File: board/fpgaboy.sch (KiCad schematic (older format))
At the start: 83 parts, among them J1 Conn_01x12, J2 Conn_01x06, J3 Micro_SD_Card_Det, J4 Conn_01x06, P1 ILI9341, P2 CONN_01X02, P3 USB_OTG, Q1 BSS816NW, SW1 SWITCH_SPST, U1 iCE40-HX8k-BG121, U2 DSC60XX, U3 GS74116AGP/, U4 BQ21040, U5 NCP1532, U6 SAML22G18A

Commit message: Connect LCD interface
Former-commit-id: be222472ea62f5be4bca7c37730c00a19e503cfb [formerly a5ab949512d659eb4659003014dfb4631add8347]
Former-commit-id: 3fc0e25a0825eb883327bfa558efda45d3fda1b2
Former-commit-id: fb121b735d250eeeb6fec0ec3e54c77ea9ad060c
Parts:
- added TP15: TestPoint, fpgaboy_parts:Testpoint_d0.7mm, symbol Connector:TestPoint
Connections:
- net labels added: LCD_D~C~
- net labels removed: LCD_D/C
- wire segments 543 -> 544
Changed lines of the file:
@@
 LCD_SCL
 Text Label 1750 8800 2    59   ~ 0
-LCD_D/C
+LCD_D~C~
 Text Label 1750 8900 2    59   ~ 0
 LCD_CS
@@
 Text Label 3300 1500 2    60   ~ 0
 SRAM_A17
+Text Label 1350 4650 2    59   ~ 0
+LCD_RESET
+Text Label 1350 4550 2    59   ~ 0
+LCD_SCL
 Text Label 1350 4350 2    59   ~ 0
-LCD_RESET
+LCD_D~C~
+Text Label 1350 4250 2    59   ~ 0
+LCD_CS
 Text Label 1350 4450 2    59   ~ 0
-LCD_SCL
-Text Label 1350 4550 2    59   ~ 0
-LCD_D/C
-Text Label 1350 4650 2    59   ~ 0
-LCD_CS
+LCD_SDA
 Text Label 1350 4750 2    59   ~ 0
-LCD_SDA
-Text Label 1350 4850 2    59   ~ 0
 LCD_SDO
 Wire Wire Line
@@
 Wire Wire Line
 	1550 4250 1350 4250
-Text Label 1350 4250 2    50   ~ 0
+Text Label 1350 4850 2    50   ~ 0
 LCD_PWM
 Wire Wire Line
@@
 Wire Wire Line
 	3700 8950 3650 8950
-Text Label 3650 8650 2    59   ~ 0
-LCD_D/C
 Text Label 3650 8800 2    59   ~ 0
 LCD_CS
@@
 Text Notes 2900 7250 0    50   ~ 0
 Note there is extensive scrambling here\nto decongest FPGA->SRAM routing
+Text Label 3650 8650 2    59   ~ 0
+LCD_D~C~
+$Comp
+L Connector:TestPoint TP15
+U 1 1 5C00C5C4
+P 3700 8350
+F 0 "TP15" V 3654 8538 50  0000 L CNN
+F 1 "TestPoint" V 3745 8538 50  0000 L CNN
+F 2 "fpgaboy_parts:Testpoint_d0.7mm" H 3900 8350 50  0001 C CNN
+F 3 "~" H 3900 8350 50  0001 C CNN
+	1    3700 8350
+	0    1    1    0
+$EndComp
+Wire Wire Line
+	3700 8350 3650 8350
+Text Label 3650 8350 2    50   ~ 0
+LCD_RESET
 $EndSCHEMATC

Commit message: More routing
Former-commit-id: bc991a0f209c43e02855cfda4d759da6902f93c3 [formerly 65e1dfea039ff2136dd6c1c80006c66a69c9e176]
Former-commit-id: 8db9430dbe284821421561ad36d1d29c18d5a661
Former-commit-id: a4f765c582eb59d9cabff1b7e73d9f24a90fca27
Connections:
- net labels removed: FPGA_CFG_SO
- wire segments 544 -> 542
- no-connect marks 52 -> 54
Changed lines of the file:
@@
 Text Label 14650 8250 0    50   ~ 0
 USB_DP
-Text Label 5300 4850 2    50   ~ 0
-FPGA_CFG_SO
 Text Label 14650 7350 0    50   ~ 0
 FPGA_CFG_SI
@@
 Text Label 14650 7250 0    50   ~ 0
 FPGA_CFG_~RST
-Text Label 14650 7650 0    50   ~ 0
-FPGA_CFG_SO
 Wire Wire Line
 	14500 7350 14650 7350
@@
 Wire Wire Line
 	14500 7550 14650 7550
-Wire Wire Line
-	14500 7650 14650 7650
 NoConn ~ 14500 5750
 NoConn ~ 14500 5850
@@
 Wire Wire Line
 	5300 5150 5700 5150
-Wire Wire Line
-	5300 4850 6100 4850
 Connection ~ 5400 4650
 Wire Wire Line
@@
 Text Label 3650 8350 2    50   ~ 0
 LCD_RESET
+NoConn ~ 6100 4850
+NoConn ~ 14500 7650
 $EndSCHEMATC

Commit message: Update PDF following pinswapping for PCB
Former-commit-id: 44465b9019a83987ad1aa7dea38d15964084dbf7 [formerly 5f61d778534b163e39ed3c2f344e42ac27f538fd]
Former-commit-id: da721d4d19a2e198d24fefeb88b35d12907259f9
Former-commit-id: 9a12214701f09df0a8f4dc57eea492204a0ea488
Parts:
- J2, J4: footprint Connector_PinHeader_1.27mm:PinHeader_1x06_P1.27mm_Vertical -> Connector_PinHeader_2.54mm:PinHeader_1x06_P2.54mm_Vertical
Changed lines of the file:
@@
 F 0 "J4" H 6600 10200 50  0000 L CNN
 F 1 "Conn_01x06" V 6700 10350 50  0000 L CNN
-F 2 "Connector_PinHeader_1.27mm:PinHeader_1x06_P1.27mm_Vertical" H 6600 10600 50  0001 C CNN
+F 2 "Connector_PinHeader_2.54mm:PinHeader_1x06_P2.54mm_Vertical" H 6600 10600 50  0001 C CNN
 F 3 "~" H 6600 10600 50  0001 C CNN
 	1    6600 10600
@@
 F 0 "J2" H 6600 9250 50  0000 L CNN
 F 1 "Conn_01x06" V 6700 9400 50  0000 L CNN
-F 2 "Connector_PinHeader_1.27mm:PinHeader_1x06_P1.27mm_Vertical" H 6600 9650 50  0001 C CNN
+F 2 "Connector_PinHeader_2.54mm:PinHeader_1x06_P2.54mm_Vertical" H 6600 9650 50  0001 C CNN
 F 3 "~" H 6600 9650 50  0001 C CNN
 	1    6600 9650

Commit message: Correct orientation of LCD connector (oops), and add rudimentary audio to board.
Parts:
- added C30: 0.1u, Capacitor_SMD:C_0603_1608Metric, symbol fpgaboy-rescue:C
- added P4: CONN_01X02, Connector_PinHeader_2.54mm:PinHeader_1x02_P2.54mm_Vertical, symbol fpgaboy-rescue:CONN_01X02
- added R13, R15: 680, Resistor_SMD:R_0603_1608Metric, symbol fpgaboy-rescue:R
- added R14: 220, Resistor_SMD:R_0603_1608Metric, symbol fpgaboy-rescue:R
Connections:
- net labels added: AUDIO_PWM
- wire segments 542 -> 559
- no-connect marks 54 -> 53
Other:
- note added: "parallel resistors are just to\navoid more unique values\n"
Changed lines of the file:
@@
 Text Label 1750 8600 2    59   ~ 0
 LCD_RESET
-Text Label 1750 8700 2    59   ~ 0
+Text Label 1750 9100 2    59   ~ 0
 LCD_SCL
-Text Label 1750 8800 2    59   ~ 0
+Text Label 1750 9000 2    59   ~ 0
 LCD_D~C~
 Text Label 1750 8900 2    59   ~ 0
 LCD_CS
-Text Label 1750 9000 2    59   ~ 0
+Text Label 1750 8800 2    59   ~ 0
 LCD_SDA
-Text Label 1750 9100 2    59   ~ 0
+Text Label 1750 8700 2    59   ~ 0
 LCD_SDO
 Text Notes 1600 8000 0    59   ~ 0
@@
 	1    0    0    -1
 $EndComp
-NoConn ~ 1550 4950
 NoConn ~ 1550 5050
 Wire Wire Line
@@
 NoConn ~ 6100 4850
 NoConn ~ 14500 7650
+Wire Wire Line
+	1550 4950 1350 4950
+Text Label 1350 4950 2    50   ~ 0
+AUDIO_PWM
+$Comp
+L fpgaboy-rescue:CONN_01X02 P4
+U 1 1 5C08551B
+P 11000 7950
+F 0 "P4" H 11000 8100 50  0000 C CNN
+F 1 "CONN_01X02" V 11100 7950 50  0000 C CNN
+F 2 "Connector_PinHeader_2.54mm:PinHeader_1x02_P2.54mm_Vertical" H 11000 7950 50  0001 C CNN
+F 3 "" H 11000 7950 50  0000 C CNN
+	1    11000 7950
+	1    0    0    -1
+$EndComp
+Wire Wire Line
+	10800 8000 10700 8000
+$Comp
+L fpgaboy-rescue:GND #PWR0102
+U 1 1 5C0DBD8A
+P 10700 8500
+F 0 "#PWR0102" H 10700 8250 50  0001 C CNN
+F 1 "GND" H 10705 8327 50  0000 C CNN
+F 2 "" H 10700 8500 50  0000 C CNN
+F 3 "" H 10700 8500 50  0000 C CNN
+	1    10700 8500
+	1    0    0    -1
+$EndComp
+$Comp
+L fpgaboy-rescue:R R15
+U 1 1 5C133D1D
+P 10400 7650
+F 0 "R15" V 10480 7650 50  0000 C CNN
+F 1 "680" V 10400 7650 50  0000 C CNN
+F 2 "Resistor_SMD:R_0603_1608Metric" V 10330 7650 50  0001 C CNN
+F 3 "" H 10400 7650 50  0000 C CNN
+	1    10400 7650
+	1    0    0    -1
+$EndComp
+$Comp
+L fpgaboy-rescue:R R13
+U 1 1 5C1342F3
+P 10150 7650
+F 0 "R13" V 10230 7650 50  0000 C CNN
+F 1 "680" V 10150 7650 50  0000 C CNN
+F 2 "Resistor_SMD:R_0603_1608Metric" V 10080 7650 50  0001 C CNN
+F 3 "" H 10150 7650 50  0000 C CNN
+	1    10150 7650
+	1    0    0    -1
+$EndComp
+$Comp
+L fpgaboy-rescue:R R14
+U 1 1 5C18A52F
+P 10150 8150
+F 0 "R14" V 10230 8150 50  0000 C CNN
+F 1 "220" V 10150 8150 50  0000 C CNN
+F 2 "Resistor_SMD:R_0603_1608Metric" V 10080 8150 50  0001 C CNN
+F 3 "" H 10150 8150 50  0000 C CNN
+	1    10150 8150
+	1    0    0    -1
+$EndComp
+$Comp
+L fpgaboy-rescue:C C30
+U 1 1 5C18A953
+P 10400 8150
+F 0 "C30" H 10425 8250 50  0000 L CNN
+F 1 "0.1u" H 10425 8050 50  0000 L CNN
+F 2 "Capacitor_SMD:C_0603_1608Metric" H 10438 8000 50  0001 C CNN
+F 3 "" H 10400 8150 50  0000 C CNN
+	1    10400 8150
+	1    0    0    -1
+$EndComp
+Wire Wire Line
+	10150 7800 10150 7900
+Wire Wire Line
+	10400 7800 10400 7900
+Wire Wire Line
+	10400 7900 10800 7900
+Connection ~ 10400 7900
+Wire Wire Line
+	10400 7900 10400 8000
+Wire Wire Line
+	10400 7900 10150 7900
+Connection ~ 10150 7900
+Wire Wire Line
+	10150 7900 10150 8000
+Wire Wire Line
+	10150 8300 10150 8400
+Wire Wire Line
+	10150 8400 10400 8400
+Wire Wire Line
+	10400 8300 10400 8400
+Wire Wire Line
+	10400 8400 10400 8500
+Connection ~ 10400 8400
+$Comp
+L fpgaboy-rescue:GND #PWR0104
+U 1 1 5C499C23
+P 10400 8500
+F 0 "#PWR0104" H 10400 8250 50  0001 C CNN
+F 1 "GND" H 10405 8327 50  0000 C CNN
+F 2 "" H 10400 8500 50  0000 C CNN
+F 3 "" H 10400 8500 50  0000 C CNN
+	1    10400 8500
+	1    0    0    -1
+$EndComp
+Wire Wire Line
+	10700 8000 10700 8500
+Wire Wire Line
+	10150 7500 10150 7400
+Wire Wire Line
+	10150 7400 9950 7400
+Wire Wire Line
+	10150 7400 10400 7400
+Wire Wire Line
+	10400 7400 10400 7500
+Connection ~ 10150 7400
+Text Label 9950 7400 2    50   ~ 0
+AUDIO_PWM
+Text Notes 10500 7550 0    50   ~ 0
+parallel resistors are just to\navoid more unique values\n
 $EndSCHEMATC

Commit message: Board changes (starting rev B): swap to 'hx4k' (actually an hx8k, but in TQ144, which is easier to solder), and add soft-latching power switch
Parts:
- removed C17: 0.1u, Capacitor_SMD:C_0603_1608Metric, symbol fpgaboy-rescue:C
- removed C18, C21: 1u, Capacitor_SMD:C_0603_1608Metric, symbol Device:C_Small
- removed C19, C22: 0.1u, Capacitor_SMD:C_0603_1608Metric, symbol Device:C_Small
- removed C3, C5: 1u, Capacitor_SMD:C_0603_1608Metric, symbol fpgaboy-rescue:C
- removed J3: Micro_SD_Card_Det, Connector_Card:microSD_HC_Hirose_DM3D-SF, symbol Connector:Micro_SD_Card_Det
- removed R12: 10k, Resistor_SMD:R_0603_1608Metric, symbol fpgaboy-rescue:R
- removed R7, R8: 10, Resistor_SMD:R_0603_1608Metric, symbol fpgaboy-rescue:R
- removed RN1, RN2, RN3, RN4: 10k, fpgaboy_parts:RN4-1206, symbol Device:R_Pack04
- removed SW1: SWITCH_SPST, fpgaboy_parts:SPDT_SLIDE_SWITCH, symbol fpgaboy_parts:SWITCH_SPST
- removed TP10, TP5, TP6, TP7, TP8, TP9: TestPoint, fpgaboy_parts:Testpoint_d0.7mm, symbol Connector:TestPoint
- removed U1: iCE40-HX8k-BG121, fpgaboy_parts:BGA-121_11x11_9.0x9.0mm, symbol fpgaboy_parts:iCE40-HX8k-BG121
- removed U6: SAML22G18A, fpgaboy_parts:QFN-48_EP_7x7_Pitch0.5mm, symbol fpgaboy_parts:SAML22G18A
- added C?: 0.1u, Capacitor_SMD:C_0603_1608Metric, symbol fpgaboy-rescue:C
- added C?: 1u, symbol Device:C_Small
- added C?: 0.1u, symbol Device:C_Small
- added R? (x2): 100k, symbol Device:R_Small
- added RN?: R_Network04, Resistor_THT:R_Array_SIP5, symbol Device:R_Network04
- added SW?: SW_Push, symbol Switch:SW_Push
- added U? (x6): iCE40-HX4K-TQ144, symbol fpgaboy_parts:iCE40-HX4K-TQ144
- added U?: W25Q16, Package_SO:SOIC-8_3.9x4.9mm_P1.27mm, symbol Memory_Flash:AT25SF081-SSHD-X
- added U? (x2): 74LVC2G04, symbol 74xGxx:74LVC2G04
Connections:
- net labels added: FLASH_IO2, FLASH_IO3, FLASH_MISO, FLASH_MOSI, FLASH_SCK, FLASH_~CS, PWR_EN
- net labels removed: VDDCORE, uSD_CLK, uSD_CMD, uSD_DAT0, uSD_DAT1, uSD_DAT2, uSD_DAT3
- wire segments 559 -> 334
- no-connect marks 53 -> 6
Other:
- note added: "Contains:\n- "bootloader" FPGA image for reprogramming flash\n- RISCBoy FPGA image\n- games"
- note added: "Power"
- note added: "QSPI Flash"
- note added: "Soft-latching Power Switch"
- note removed: "DC Connection\nGNDPLL <-> GND\nis made internally\n"
- note removed: "Micro SD Card Socket\n"
- note removed: "Microcontroller\nProvides:\n - FPGA configuration image stored in flash\n - USB <-> UART\n - USB <-> SD Card"
- note removed: "Note there is extensive scrambling here\nto decongest FPGA->SRAM routing"
- note removed: "SPI Mode:\nCMD -> MOSI\nCLK -> SCLK\nDAT3 -> ~SS~\nDAT0 -> MISO\n"
- note removed: "SPI Mode:\nDAT3 -> ~SS~\nCLK -> SCLK\nCMD -> MOSI\nDAT0 -> MISO"
- moved on the sheet: C14, C15, C16, C20, C23, C24, C25, C26, C27, C28, C29, C30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

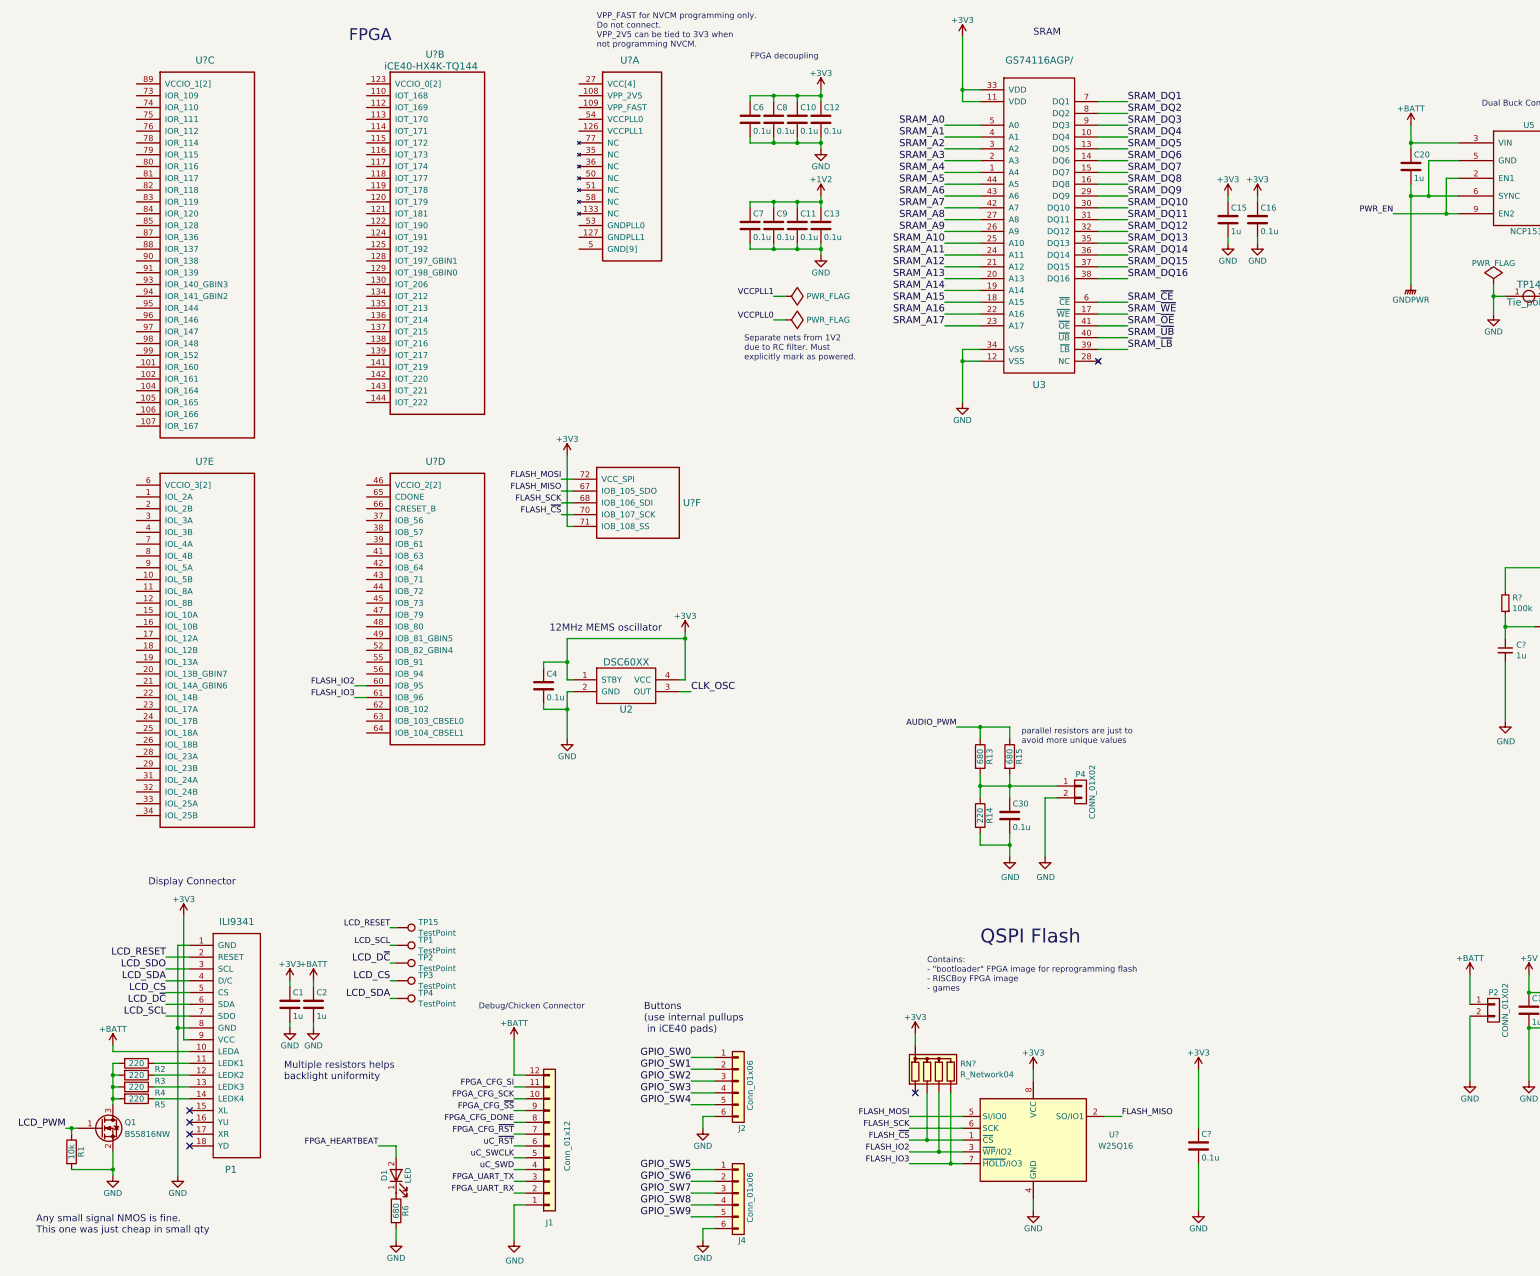
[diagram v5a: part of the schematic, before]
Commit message: Create symbol for QFN20 version of CP2102 USB-serial bridge. Add this to schematic.
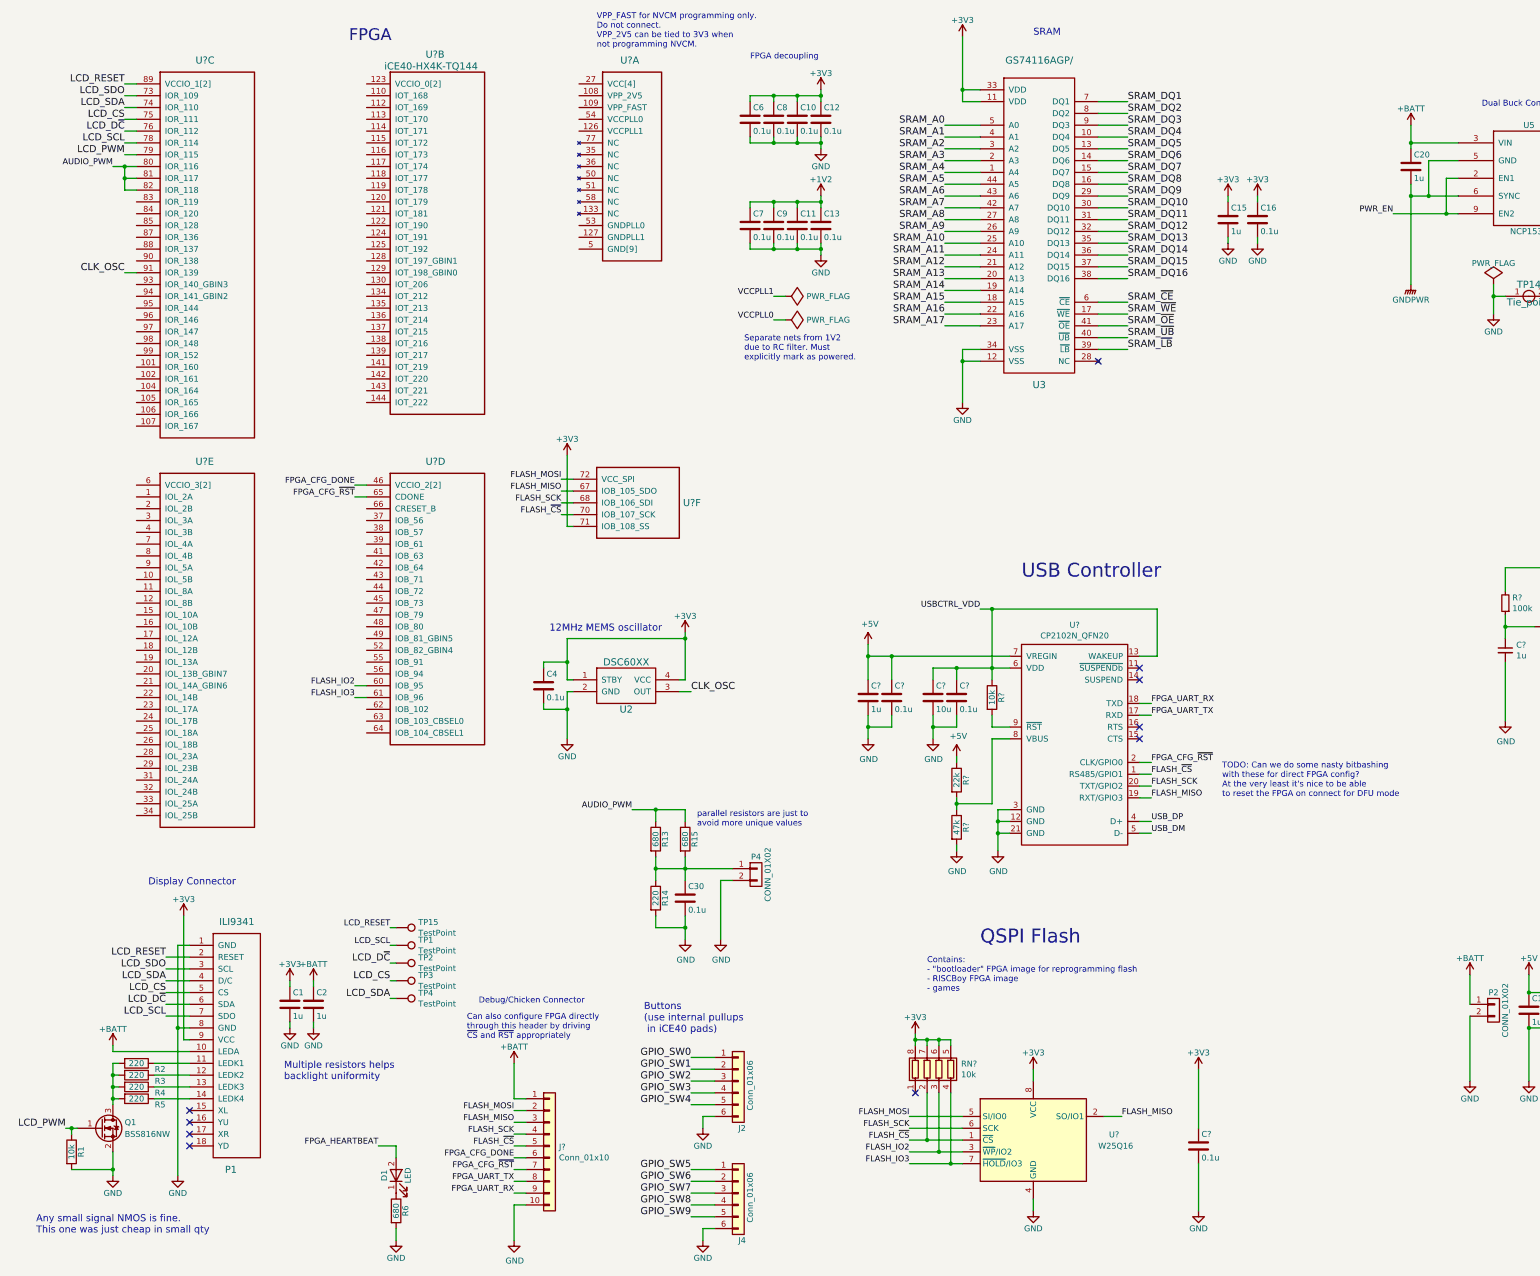
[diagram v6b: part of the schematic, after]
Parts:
- removed J1: Conn_01x12, Connector_PinHeader_2.54mm:PinHeader_1x12_P2.54mm_Horizontal, symbol Connector_Generic:Conn_01x12
- removed RN?: R_Network04, Resistor_THT:R_Array_SIP5, symbol Device:R_Network04
- added C? (x2): 0.1u, Capacitor_SMD:C_0603_1608Metric, symbol fpgaboy-rescue:C
- added C?: 1u, Capacitor_SMD:C_0603_1608Metric, symbol fpgaboy-rescue:C
- added C?: 10u, Capacitor_SMD:C_0603_1608Metric, symbol fpgaboy-rescue:C
- added J?: Conn_01x10, symbol Connector_Generic:Conn_01x10
- added R?: 10k, Resistor_SMD:R_0603_1608Metric, symbol fpgaboy-rescue:R
- added R?: 22k, Resistor_SMD:R_0603_1608Metric, symbol fpgaboy-rescue:R
- added R?: 47k, Resistor_SMD:R_0603_1608Metric, symbol fpgaboy-rescue:R
- added RN?: 10k, symbol Device:R_Pack04
- added U?: CP2102N_QFN20, symbol fpgaboy_parts:CP2102N_QFN20
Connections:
- net +3V3: now also RN?.5 (R4.2), RN?.6 (R3.2), RN?.7 (R2.2), RN?.8 (R1.2)
- net +5V: now also C?.1, C?.1, R?.1, U?.7 (VREGIN)
- net +BATT: now also J?.1 (Pin_1)
- net AUDIO_PWM: now also U?.80 (IOR_116), U?.81 (IOR_117), U?.82 (IOR_118)
- net CLK_OSC: now also U?.91 (IOR_139)
- net FLASH_IO2: now also RN?.3 (R3.1)
- net FLASH_IO3: now also RN?.4 (R4.1)
- net FLASH_MISO: now also J?.3 (Pin_3), U?.19 (RXT/GPIO3)
- net FLASH_MOSI: now also J?.2 (Pin_2)
- net FLASH_SCK: now also J?.4 (Pin_4), U?.20 (TXT/GPIO2)
- net FLASH_~CS: now also J?.5 (Pin_5), RN?.2 (R2.1), U?.1 (RS485/GPIO1)
- net FPGA_CFG_DONE: now also U?.46 (VCCIO_2[2]), U?.57 (VCCIO_2[2]), J?.6 (Pin_6)
- net FPGA_CFG_~RST: now also U?.65 (CDONE), J?.7 (Pin_7), U?.2 (CLK/GPIO0)
- net FPGA_UART_RX: now also J?.9 (Pin_9), U?.18 (TXD)
- net FPGA_UART_TX: now also J?.8 (Pin_8), U?.17 (RXD)
- net GND: now also C?.2, C?.2, C?.2, C?.2, J?.10 (Pin_10), R?.2, U?.12 (GND), U?.21 (GND), U?.3 (GND)
- net LCD_CS: now also U?.75 (IOR_111)
- net LCD_D~C~: now also U?.76 (IOR_112)
- net LCD_PWM: now also U?.79 (IOR_115)
- net LCD_RESET: now also U?.100 (VCCIO_1[2]), U?.89 (VCCIO_1[2])
- net LCD_SCL: now also U?.78 (IOR_114)
- net LCD_SDA: now also U?.74 (IOR_110)
- net LCD_SDO: now also U?.73 (IOR_109)
- net USB_DM: now also U?.5 (D-)
- net USB_DP: now also U?.4 (D+)
- new net: R?.1, R?.2, U?.8 (VBUS)
- new net: R?.2, U?.9 (~RST)
- new net USBCTRL_VDD: C?.1, C?.1, R?.1, U?.13 (WAKEUP), U?.6 (VDD)
- no-connect marks 6 -> 10
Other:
- note added: "Can also configure FPGA directly\nthrough this header by driving\n~CS~ and ~RST~ appropriately"
- note added: "TODO: Can we do some nasty bitbashing\nwith these for direct FPGA config?\nAt the very least it's nice to be able\nto reset the FPGA on connect for DFU mode"
- note added: "USB Controller"
- moved on the sheet: C30, P4, R13, R14, R15
